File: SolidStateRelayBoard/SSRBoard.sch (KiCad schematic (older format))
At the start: 49 parts, among them J101 CONN_01X02, J102 CONN_01X02, J103 CONN_01X02, J104 CONN_01X02, J105 CONN_01X02, J106 CONN_01X02, J107 CONN_01X02, J108 CONN_01X02, J109 CONN_01X02, J110 CONN_01X02, J111 CONN_01X02, J112 CONN_01X02, J113 CONN_01X02, J114 CONN_01X02, J115 CONN_01X02, J116 CONN_01X02, J117 CONN_01X02, J118 CONN_01X02, J119 CONN_01X02, J120 CONN_01X02, J121 CONN_01X02, J122 CONN_01X02, J123 CONN_01X02, J124 CONN_01X02, J125 CONN_01X02, J126 CONN_01X02, J127 CONN_01X02, J128 CONN_01X02, J129 CONN_01X02, J130 CONN_01X02, J131 CONN_01X02, J132 CONN_01X02, J133 CONN_01X02, J134 CONN_01X16

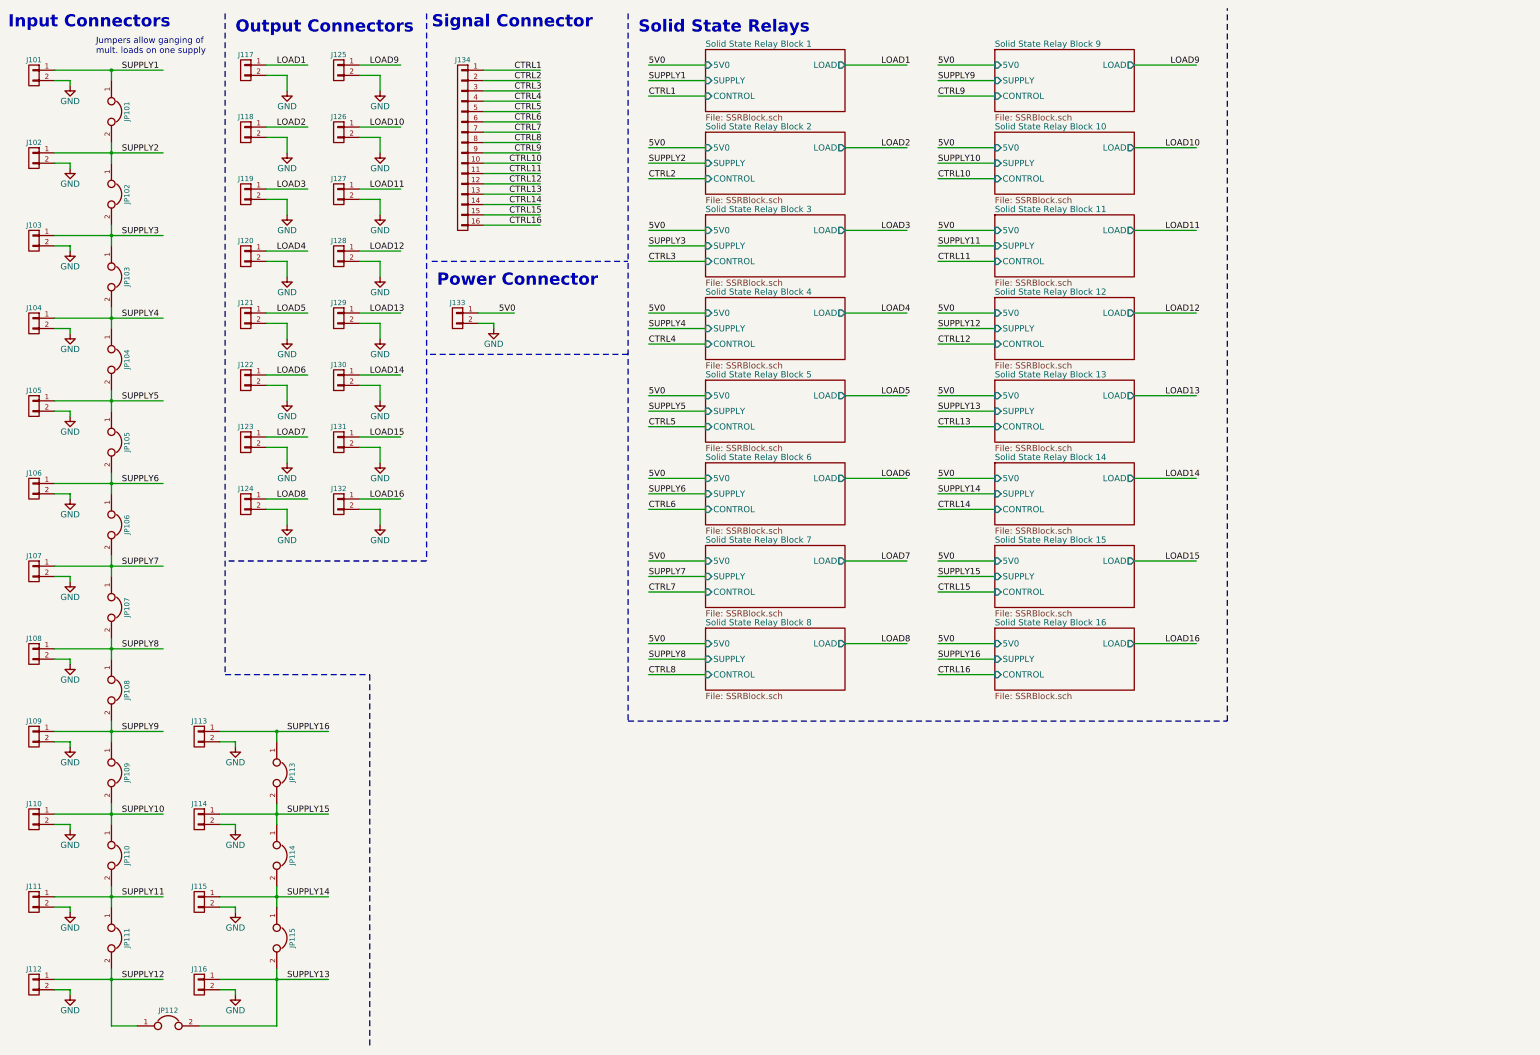
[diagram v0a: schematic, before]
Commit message: Completed most of layout for SSR board.
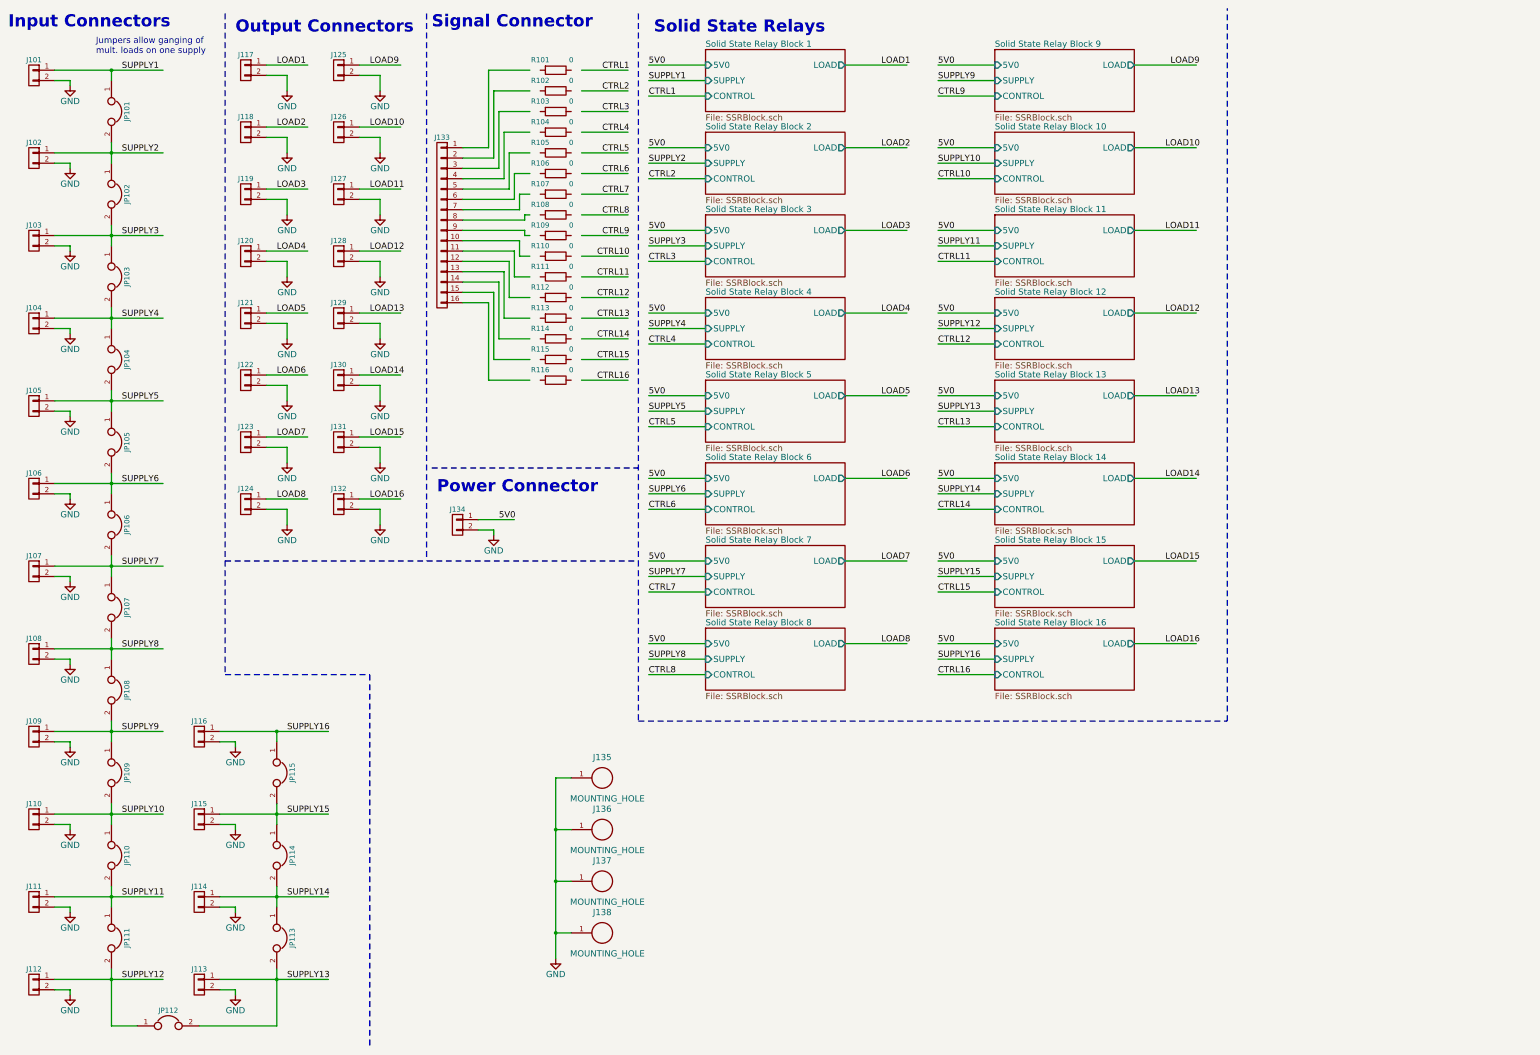
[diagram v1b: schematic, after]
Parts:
- added J135, J136, J137, J138: MOUNTING_HOLE, hyperCustom:MountingHole_5.5mm_Pad_Via, symbol MOUNTING_HOLE
- added R101, R102, R103, R104, R105, R106, R107, R108, R109, R110, R111, R112, R113, R114, R115, R116: 0, Resistors_SMD:R_1206_HandSoldering, symbol R
- J133: renamed from J134; footprint (none) -> hyperCustom:CONN_PHOENIX_1844359_16PIN
- renumbered J116 to J113, J115 to J114, J114 to J115, J113 to J116, J133 to J134, JP115 to JP113, JP113 to JP115
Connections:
- wire segments 197 -> 250
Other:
- moved on the sheet: J133, J134

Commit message: Deleted some of the unnecessary circuits for the relays that won’t be used anymore since we will have two boards now.
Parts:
- R101, R102, R103, R104, R105, R106, R107, R108, R109, R110, R111, R112, R113, R114, R115, R116: symbol R -> R-RESCUE-SSRBoard
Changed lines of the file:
@@
 EESchema Schematic File Version 2
+LIBS:SSRBoard-rescue
 LIBS:transistors
 LIBS:device
@@
 LIBS:silabs
 LIBS:siliconi
-LIBS:special
 LIBS:stm8
 LIBS:stm32
@@
 $EndComp
 $Comp
-L R R101
+L R-RESCUE-SSRBoard R101
 U 1 1 586C9ADD
 P 5800 1050
@@
 $EndComp
 $Comp
-L R R102
+L R-RESCUE-SSRBoard R102
 U 1 1 586CA945
 P 5800 1250
@@
 $EndComp
 $Comp
-L R R103
+L R-RESCUE-SSRBoard R103
 U 1 1 586CAB74
 P 5800 1450
@@
 $EndComp
 $Comp
-L R R104
+L R-RESCUE-SSRBoard R104
 U 1 1 586CADA6
 P 5800 1650
@@
 $EndComp
 $Comp
-L R R105
+L R-RESCUE-SSRBoard R105
 U 1 1 586CB2BA
 P 5800 1850
@@
 $EndComp
 $Comp
-L R R106
+L R-RESCUE-SSRBoard R106
 U 1 1 586CB4F2
 P 5800 2050
@@
 $EndComp
 $Comp
-L R R107
+L R-RESCUE-SSRBoard R107
 U 1 1 586CB72D
 P 5800 2250
@@
 $EndComp
 $Comp
-L R R108
+L R-RESCUE-SSRBoard R108
 U 1 1 586CB96B
 P 5800 2450
@@
 $EndComp
 $Comp
-L R R109
+L R-RESCUE-SSRBoard R109
 U 1 1 586CCFBF
 P 5800 2650
@@
 $EndComp
 $Comp
-L R R110
+L R-RESCUE-SSRBoard R110
 U 1 1 586CCFC8
 P 5800 2850
@@
 $EndComp
 $Comp
-L R R111
+L R-RESCUE-SSRBoard R111
 U 1 1 586CCFD1
 P 5800 3050
@@
 $EndComp
 $Comp
-L R R112
+L R-RESCUE-SSRBoard R112
 U 1 1 586CCFDA
 P 5800 3250
@@
 $EndComp
 $Comp
-L R R113
+L R-RESCUE-SSRBoard R113
 U 1 1 586CCFE3
 P 5800 3450
@@
 $EndComp
 $Comp
-L R R114
+L R-RESCUE-SSRBoard R114
 U 1 1 586CCFEC
 P 5800 3650
@@
 $EndComp
 $Comp
-L R R115
+L R-RESCUE-SSRBoard R115
 U 1 1 586CCFF5
 P 5800 3850
@@
 $EndComp
 $Comp
-L R R116
+L R-RESCUE-SSRBoard R116
 U 1 1 586CCFFE
 P 5800 4050

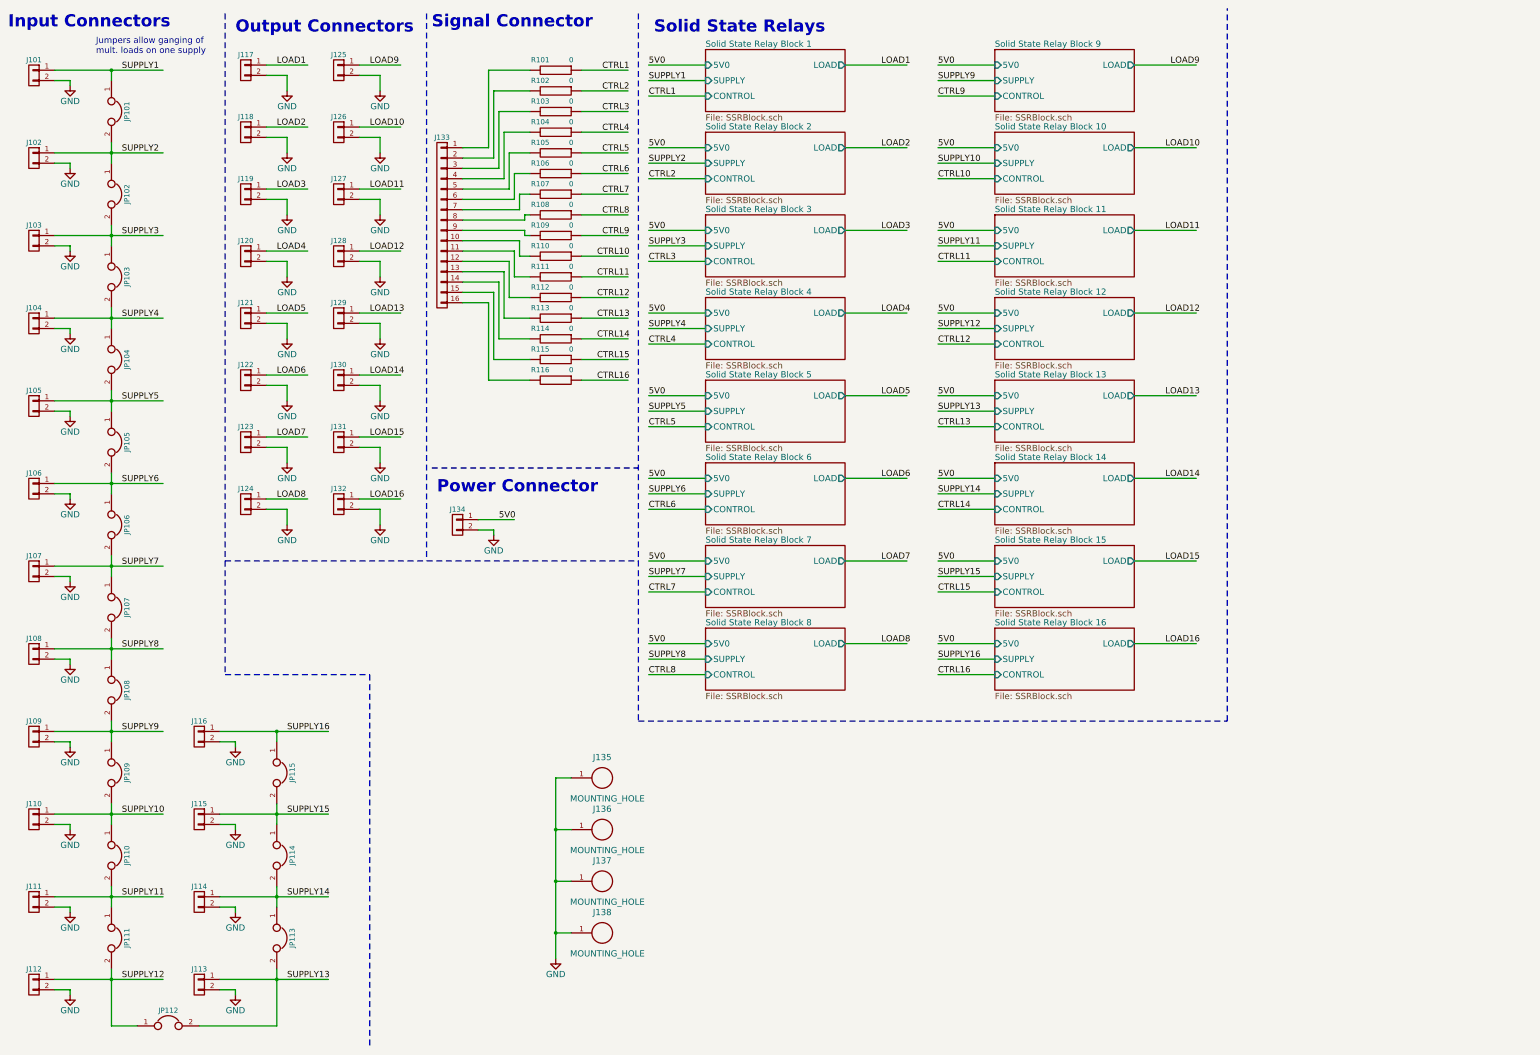
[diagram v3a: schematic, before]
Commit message: Added the LED driver IC to the schematic and started making the changes necessary to the PCB
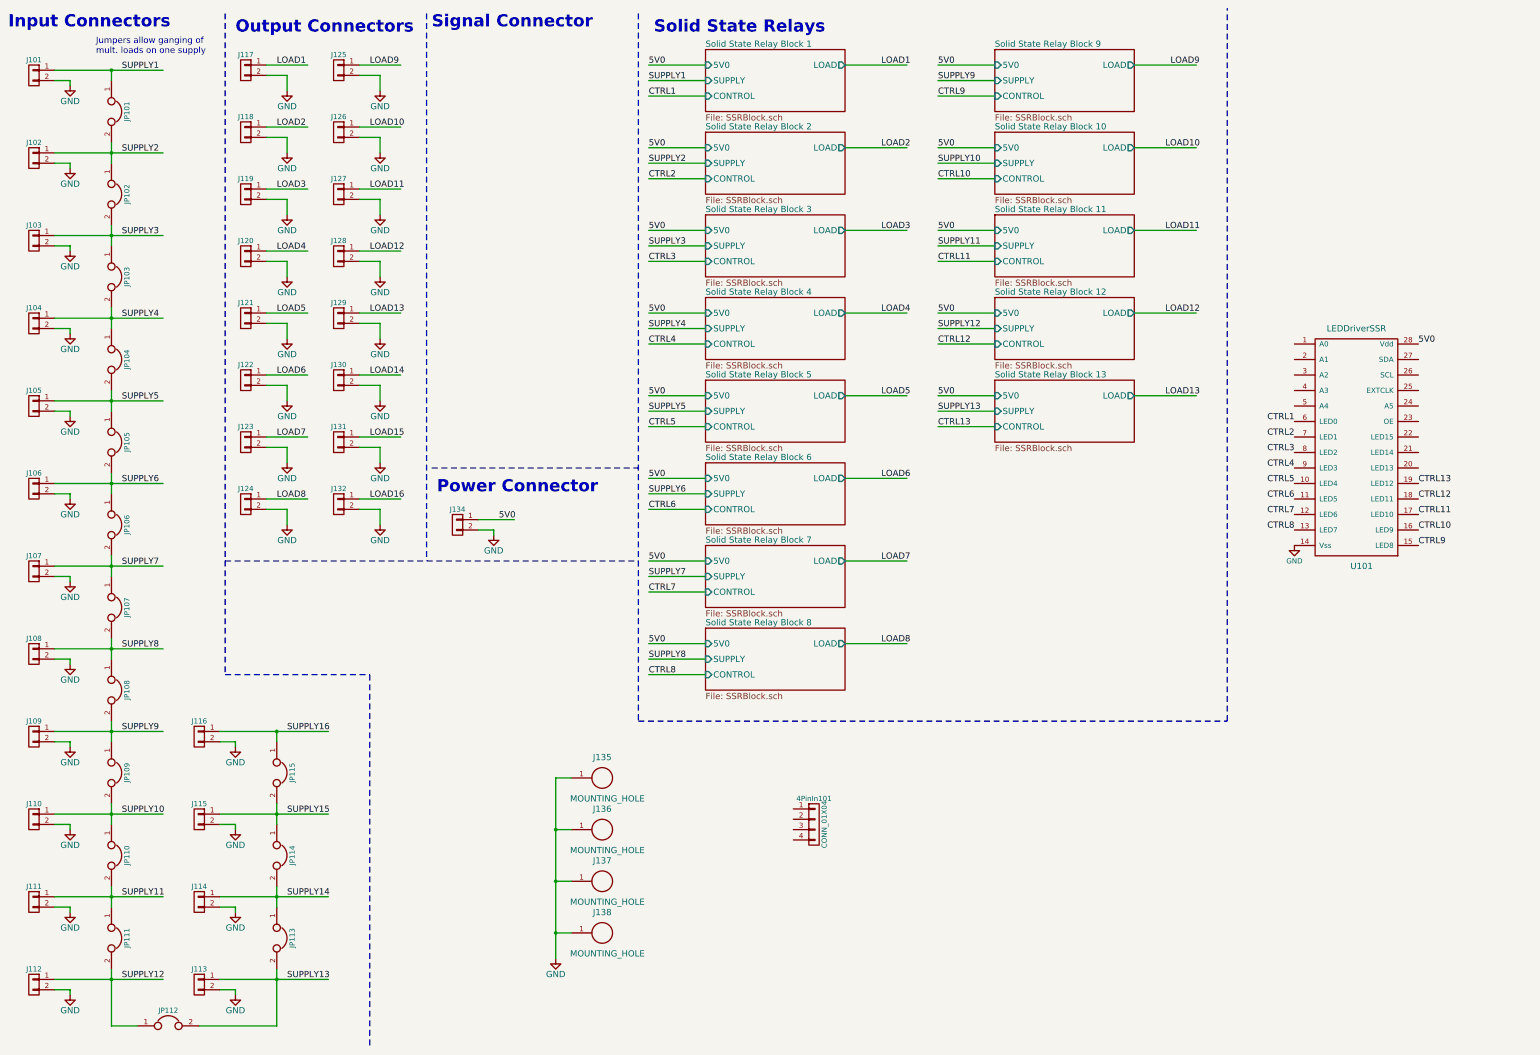
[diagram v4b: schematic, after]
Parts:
- removed J133: CONN_01X16, hyperCustom:CONN_PHOENIX_1844359_16PIN, symbol CONN_01X16
- removed R101, R102, R103, R104, R105, R106, R107, R108, R109, R110, R111, R112, R113, R114, R115, R116: 0, Resistors_SMD:R_1206_HandSoldering, symbol R-RESCUE-SSRBoard
- added 4PinIn101: CONN_01X04, symbol CONN_01X04
- added U101: LEDDriverSSR, Housings_SSOP:TSSOP-28_4.4x9.7mm_Pitch0.65mm, symbol LEDDriverSSR
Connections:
- net labels removed: CTRL14, CTRL15, CTRL16
- wire segments 250 -> 174
